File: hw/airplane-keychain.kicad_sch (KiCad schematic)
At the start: 19 parts, among them J1 CONN_01X03_MALE, SW1 SW_PUSH, SW2 SPST, U1 ATtiny85-20P

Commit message: Initial update for ISGC model
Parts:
- added R7, R8, R9: 100, Resistor_THT:R_Axial_DIN0309_L9.0mm_D3.2mm_P12.70mm_Horizontal, symbol airplane-keychain-rescue:R
- BT1, BT2: footprint Battery_Holders:Keystone_1058_1x2032-CoinCell -> Battery:BatteryHolder_Keystone_1058_1x2032
- D1: footprint LEDs:LED_D5.0mm -> LED_THT:LED_D3.0mm
- D2, D5, D6: footprint LEDs:LED_1206 -> LED_THT:LED_D3.0mm
- D3, D4: footprint LEDs:LED_D3.0mm_Horizontal_O1.27mm_Z2.0mm -> LED_THT:LED_D3.0mm
- D7: footprint LEDs:LED_D5.0mm_Horizontal_O1.27mm_Z3.0mm -> LED_THT:LED_D3.0mm
- J1: footprint Pin_Headers:Pin_Header_Straight_1x03_Pitch2.54mm -> Connector_PinHeader_2.54mm:PinHeader_1x03_P2.54mm_Horizontal
- R1, R2, R3, R4, R5, R6: footprint Resistors_THT:R_Axial_DIN0309_L9.0mm_D3.2mm_P12.70mm_Horizontal -> Resistor_THT:R_Axial_DIN0309_L9.0mm_D3.2mm_P12.70mm_Horizontal
- SW1: footprint Buttons_Switches_THT:SW_PUSH_6mm -> Button_Switch_THT:SW_PUSH_6mm
- SW2: footprint Buttons_Switches_THT:SW_Micro_SPST -> Button_Switch_THT:SW_DIP_SPSTx01_Slide_9.78x4.72mm_W7.62mm_P2.54mm
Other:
- title: Airplane Keychain -> ISGC Keychain
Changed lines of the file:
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@@
   (paper "A4")
   (title_block
-    (title "Airplane Keychain")
-    (date "2023-04-15")
-    (rev "B")
+    (title "ISGC Keychain")
+    (date "2023-12-07")
+    (rev "C")
     (company "Make to Innovate")
     (comment 1 "Matthew E. Nelson")
-    (comment 2 "High Wing PCB design")
+    (comment 2 "ISGC Badge")
   )
   (junction (at 40.64 80.01) (diameter 0) (color 0 0 0 0)
@@
       (effects (font (size 1.27 1.27)))
     )
-    (property "Footprint" "LEDs:LED_D5.0mm" (at 55.88 50.8 0)
+    (property "Footprint" "LED_THT:LED_D3.0mm" (at 55.88 50.8 0)
       (effects (font (size 1.27 1.27)) hide)
     )
@@
       (effects (font (size 1.27 1.27)))
     )
-    (property "Footprint" "LEDs:LED_1206" (at 55.88 59.69 0)
+    (property "Footprint" "LED_THT:LED_D3.0mm" (at 55.88 59.69 0)
       (effects (font (size 1.27 1.27)) hide)
     )
@@
       (effects (font (size 1.27 1.27)))
     )
-    (property "Footprint" "LEDs:LED_D3.0mm_Horizontal_O1.27mm_Z2.0mm" (at 55.88 71.12 0)
+    (property "Footprint" "LED_THT:LED_D3.0mm" (at 55.88 71.12 0)
       (effects (font (size 1.27 1.27)) hide)
     )
@@
       (effects (font (size 1.27 1.27)))
     )
-    (property "Footprint" "LEDs:LED_D3.0mm_Horizontal_O1.27mm_Z2.0mm" (at 55.88 80.01 0)
+    (property "Footprint" "LED_THT:LED_D3.0mm" (at 55.88 80.01 0)
       (effects (font (size 1.27 1.27)) hide)
     )
@@
       (effects (font (size 1.27 1.27)))
     )
-    (property "Footprint" "LEDs:LED_1206" (at 55.88 93.98 0)
+    (property "Footprint" "LED_THT:LED_D3.0mm" (at 55.88 93.98 0)
       (effects (font (size 1.27 1.27)) hide)
     )
@@
       (effects (font (size 1.27 1.27)))
     )
-    (property "Footprint" "LEDs:LED_1206" (at 55.88 102.87 0)
+    (property "Footprint" "LED_THT:LED_D3.0mm" (at 55.88 102.87 0)
       (effects (font (size 1.27 1.27)) hide)
     )
@@
       (effects (font (size 1.27 1.27)))
     )
-    (property "Footprint" "LEDs:LED_D5.0mm_Horizontal_O1.27mm_Z3.0mm" (at 55.88 116.84 0)
+    (property "Footprint" "LED_THT:LED_D3.0mm" (at 55.88 116.84 0)
       (effects (font (size 1.27 1.27)) hide)
     )
@@
       (effects (font (size 1.27 1.27)))
     )
-    (property "Footprint" "Buttons_Switches_THT:SW_PUSH_6mm" (at 106.68 116.84 0)
+    (property "Footprint" "Button_Switch_THT:SW_PUSH_6mm" (at 106.68 116.84 0)
       (effects (font (size 1.27 1.27)) hide)
     )
@@
       (effects (font (size 1.27 1.27)))
     )
-    (property "Footprint" "Buttons_Switches_THT:SW_Micro_SPST" (at 220.98 87.63 0)
+    (property "Footprint" "Button_Switch_THT:SW_DIP_SPSTx01_Slide_9.78x4.72mm_W7.62mm_P2.54mm" (at 220.98 87.63 0)
       (effects (font (size 1.27 1.27)) hide)
     )
@@
       (effects (font (size 1.27 1.27)))
     )
-    (property "Footprint" "Resistors_THT:R_Axial_DIN0309_L9.0mm_D3.2mm_P12.70mm_Horizontal" (at 74.93 49.022 90)
+    (property "Footprint" "Resistor_THT:R_Axial_DIN0309_L9.0mm_D3.2mm_P12.70mm_Horizontal" (at 74.93 49.022 90)
       (effects (font (size 1.27 1.27)) hide)
     )
@@
       (effects (font (size 1.27 1.27)))
     )
-    (property "Footprint" "Resistors_THT:R_Axial_DIN0309_L9.0mm_D3.2mm_P12.70mm_Horizontal" (at 74.93 57.912 90)
+    (property "Footprint" "Resistor_THT:R_Axial_DIN0309_L9.0mm_D3.2mm_P12.70mm_Horizontal" (at 74.93 57.912 90)
       (effects (font (size 1.27 1.27)) hide)
     )
@@
       (effects (font (size 1.27 1.27)))
     )
-    (property "Footprint" "Resistors_THT:R_Axial_DIN0309_L9.0mm_D3.2mm_P12.70mm_Horizontal" (at 74.93 69.342 90)
+    (property "Footprint" "Resistor_THT:R_Axial_DIN0309_L9.0mm_D3.2mm_P12.70mm_Horizontal" (at 74.93 69.342 90)
       (effects (font (size 1.27 1.27)) hide)
     )
@@
       (effects (font (size 1.27 1.27)))
     )
-    (property "Footprint" "Resistors_THT:R_Axial_DIN0309_L9.0mm_D3.2mm_P12.70mm_Horizontal" (at 74.93 78.232 90)
+    (property "Footprint" "Resistor_THT:R_Axial_DIN0309_L9.0mm_D3.2mm_P12.70mm_Horizontal" (at 74.93 78.232 90)
       (effects (font (size 1.27 1.27)) hide)
     )
@@
       (effects (font (size 1.27 1.27)))
     )
-    (property "Footprint" "Resistors_THT:R_Axial_DIN0309_L9.0mm_D3.2mm_P12.70mm_Horizontal" (at 74.93 115.062 90)
+    (property "Footprint" "Resistor_THT:R_Axial_DIN0309_L9.0mm_D3.2mm_P12.70mm_Horizontal" (at 74.93 115.062 90)
       (effects (font (size 1.27 1.27)) hide)
     )
@@
       (effects (font (size 1.27 1.27)) (justify left))
     )
-    (property "Footprint" "Battery_Holders:Keystone_1058_1x2032-CoinCell" (at 234.95 117.856 90)
+    (property "Footprint" "Battery:BatteryHolder_Keystone_1058_1x2032" (at 234.95 117.856 90)
       (effects (font (size 1.27 1.27)) hide)
     )
@@
       (effects (font (size 1.27 1.27)) (justify left))
     )
-    (property "Footprint" "Battery_Holders:Keystone_1058_1x2032-CoinCell" (at 220.98 117.856 90)
+    (property "Footprint" "Battery:BatteryHolder_Keystone_1058_1x2032" (at 220.98 117.856 90)
       (effects (font (size 1.27 1.27)) hide)
     )
@@
       (effects (font (size 1.27 1.27)))
     )
-    (property "Footprint" "Pin_Headers:Pin_Header_Straight_1x03_Pitch2.54mm" (at 48.26 26.67 0)
+    (property "Footprint" "Connector_PinHeader_2.54mm:PinHeader_1x03_P2.54mm_Horizontal" (at 48.26 26.67 0)
       (effects (font (size 1.27 1.27)) hide)
     )
@@
       (effects (font (size 1.27 1.27)))
     )
-    (property "Footprint" "Resistors_THT:R_Axial_DIN0309_L9.0mm_D3.2mm_P12.70mm_Horizontal" (at 161.29 99.822 90)
+    (property "Footprint" "Resistor_THT:R_Axial_DIN0309_L9.0mm_D3.2mm_P12.70mm_Horizontal" (at 161.29 99.822 90)
       (effects (font (size 1.27 1.27)) hide)
     )
@@
         (path "/6cfc2c66-5048-4a9e-b97d-b82fde315677"
           (reference "R6") (unit 1)
+        )
+      )
+    )
+  )
+  (symbol (lib_id "airplane-keychain-rescue:R") (at 73.66 105.41 270) (unit 1)
+    (in_bom yes) (on_board yes) (dnp no)
+    (property "Reference" "R8" (at 73.66 107.442 90)
+      (effects (font (size 1.27 1.27)))
+    )
+    (property "Value" "100" (at 73.66 105.41 90)
+      (effects (font (size 1.27 1.27)))
+    )
+    (property "Footprint" "Resistor_THT:R_Axial_DIN0309_L9.0mm_D3.2mm_P12.70mm_Horizontal" (at 73.66 103.632 90)
+      (effects (font (size 1.27 1.27)) hide)
+    )
+    (property "Datasheet" "" (at 73.66 105.41 0)
+      (effects (font (size 1.27 1.27)) hide)
+    )
+    (pin "1")
+    (pin "2")
+    (instances
+      (project "airplane-keychain"
+        (path "/6cfc2c66-5048-4a9e-b97d-b82fde315677"
+          (reference "R8") (unit 1)
+        )
+      )
+    )
+  )
+  (symbol (lib_id "airplane-keychain-rescue:R") (at 74.93 123.19 270) (unit 1)
+    (in_bom yes) (on_board yes) (dnp no)
+    (property "Reference" "R9" (at 74.93 125.222 90)
+      (effects (font (size 1.27 1.27)))
+    )
+    (property "Value" "100" (at 74.93 123.19 90)
+      (effects (font (size 1.27 1.27)))
+    )
+    (property "Footprint" "Resistor_THT:R_Axial_DIN0309_L9.0mm_D3.2mm_P12.70mm_Horizontal" (at 74.93 121.412 90)
+      (effects (font (size 1.27 1.27)) hide)
+    )
+    (property "Datasheet" "" (at 74.93 123.19 0)
+      (effects (font (size 1.27 1.27)) hide)
+    )
+    (pin "1")
+    (pin "2")
+    (instances
+      (project "airplane-keychain"
+        (path "/6cfc2c66-5048-4a9e-b97d-b82fde315677"
+          (reference "R9") (unit 1)
         )
       )
@@
         )
       )
+    )
+  )
+  (symbol (lib_id "airplane-keychain-rescue:R") (at 72.39 91.44 270) (unit 1)
+    (in_bom yes) (on_board yes) (dnp no)
+    (property "Reference" "R7" (at 72.39 93.472 90)
+      (effects (font (size 1.27 1.27)))
+    )
+    (property "Value" "100" (at 72.39 91.44 90)
+      (effects (font (size 1.27 1.27)))
+    )
+    (property "Footprint" "Resistor_THT:R_Axial_DIN0309_L9.0mm_D3.2mm_P12.70mm_Horizontal" (at 72.39 89.662 90)
+      (effects (font (size 1.27 1.27)) hide)
+    )
+    (property "Datasheet" "" (at 72.39 91.44 0)
+      (effects (font (size 1.27 1.27)) hide)
+    )
+    (pin "1")
+    (pin "2")
+    (instances
+      (project "airplane-keychain"
+        (path "/6cfc2c66-5048-4a9e-b97d-b82fde315677"
+          (reference "R7") (unit 1)
+        )
+      )

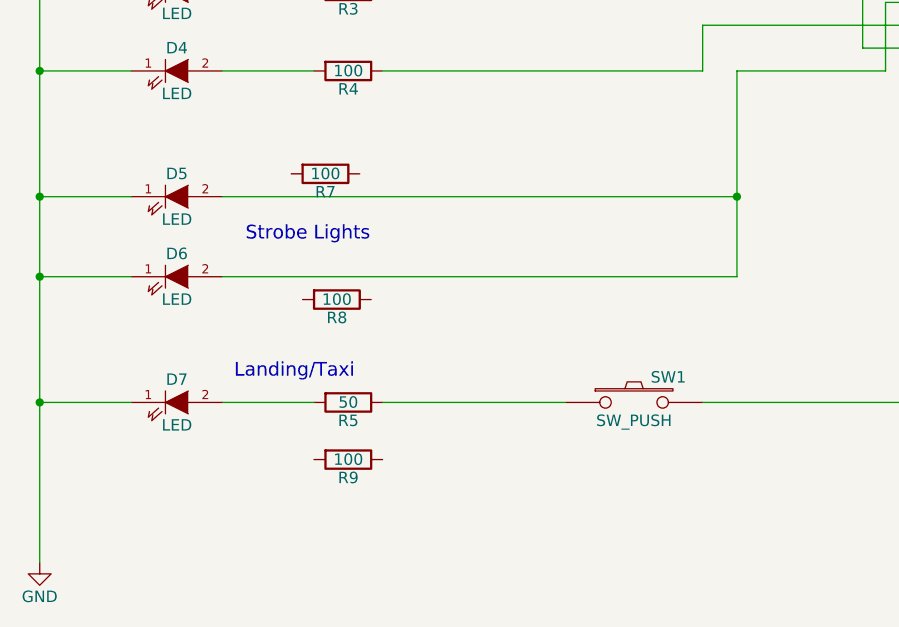
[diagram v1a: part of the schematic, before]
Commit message: Updates to logo
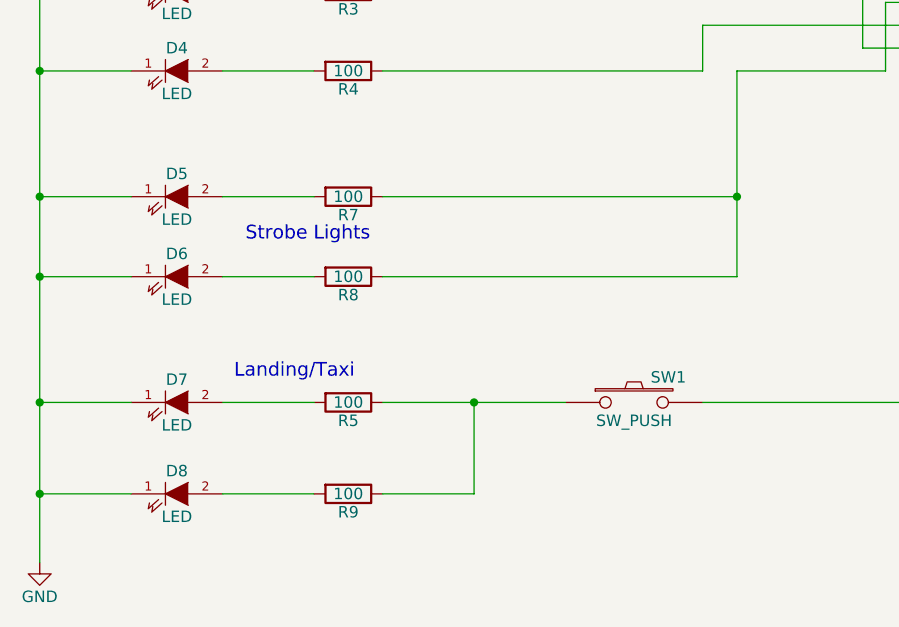
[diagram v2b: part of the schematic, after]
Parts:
- added D8: LED, LED_THT:LED_D3.0mm, symbol airplane-keychain-rescue:LED-RESCUE-airplane-keychain
- R5: value 50 -> 100
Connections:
- net GND: now also D8.1 (K)
- net at R5.1, SW1.1: now also R9.1
- net at R8.1: now also R7.1, U1.3 (XTAL2/PB4)
- net at R8.2: now also D6.2 (A)
- net at R9.2: now also D8.2 (A)
- net at R7.2: now also D5.2 (A)
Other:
- moved on the sheet: R7, R8, R9

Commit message: Update for ISGC
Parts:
- removed J1: CONN_01X03_MALE, Connector_PinHeader_2.54mm:PinHeader_1x03_P2.54mm_Horizontal, symbol airplane-keychain-rescue:CONN_01X03_MALE
- added H1: MountingHole, MountingHole:MountingHole_4.3mm_M4, symbol Mechanical:MountingHole
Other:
- note removed: "Optional Tail Header"
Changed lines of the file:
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@@
   (junction (at 40.64 80.01) (diameter 0) (color 0 0 0 0)
   )
-  (junction (at 63.5 50.8) (diameter 0) (color 0 0 0 0)
-  )
   (junction (at 40.64 59.69) (diameter 0) (color 0 0 0 0)
   )
@@
   (junction (at 40.64 71.12) (diameter 0) (color 0 0 0 0)
   )
-  (junction (at 40.64 50.8) (diameter 0) (color 0 0 0 0)
-  )
   (junction (at 118.11 93.98) (diameter 0) (color 0 0 0 0)
   )
@@
   (junction (at 40.64 93.98) (diameter 0) (color 0 0 0 0)
   )
-  (junction (at 68.58 59.69) (diameter 0) (color 0 0 0 0)
-  )
   (junction (at 220.98 107.95) (diameter 0) (color 0 0 0 0)
   )
@@
     (stroke (width 0) (type default))
   )
-  (wire (pts (xy 60.96 50.8) (xy 63.5 50.8))
+  (wire (pts (xy 60.96 50.8) (xy 71.12 50.8))
     (stroke (width 0) (type default))
   )
@@
     (stroke (width 0) (type default))
   )
-  (wire (pts (xy 55.88 31.75) (xy 58.42 31.75))
-    (stroke (width 0) (type default))
-  )
   (wire (pts (xy 118.11 93.98) (xy 118.11 102.87))
     (stroke (width 0) (type default))
@@
     (stroke (width 0) (type default))
   )
-  (wire (pts (xy 55.88 36.83) (xy 63.5 36.83))
-    (stroke (width 0) (type default))
-  )
   (wire (pts (xy 132.08 77.47) (xy 132.08 71.12))
     (stroke (width 0) (type default))
@@
     (stroke (width 0) (type default))
   )
-  (wire (pts (xy 63.5 36.83) (xy 63.5 50.8))
-    (stroke (width 0) (type default))
-  )
   (wire (pts (xy 207.01 90.17) (xy 207.01 101.6))
     (stroke (width 0) (type default))
@@
     (stroke (width 0) (type default))
   )
-  (wire (pts (xy 58.42 31.75) (xy 58.42 34.29))
-    (stroke (width 0) (type default))
-  )
   (wire (pts (xy 146.05 77.47) (xy 132.08 77.47))
     (stroke (width 0) (type default))
@@
     (stroke (width 0) (type default))
   )
-  (wire (pts (xy 60.96 59.69) (xy 68.58 59.69))
+  (wire (pts (xy 60.96 59.69) (xy 71.12 59.69))
     (stroke (width 0) (type default))
   )
@@
     (stroke (width 0) (type default))
   )
-  (wire (pts (xy 55.88 26.67) (xy 68.58 26.67))
-    (stroke (width 0) (type default))
-  )
-  (wire (pts (xy 40.64 34.29) (xy 40.64 50.8))
-    (stroke (width 0) (type default))
-  )
   (wire (pts (xy 78.74 71.12) (xy 132.08 71.12))
     (stroke (width 0) (type default))
   )
-  (wire (pts (xy 68.58 26.67) (xy 68.58 59.69))
-    (stroke (width 0) (type default))
-  )
   (wire (pts (xy 161.29 54.61) (xy 161.29 59.69))
     (stroke (width 0) (type default))
@@
     (stroke (width 0) (type default))
   )
-  (wire (pts (xy 68.58 59.69) (xy 71.12 59.69))
-    (stroke (width 0) (type default))
-  )
   (wire (pts (xy 165.1 101.6) (xy 207.01 101.6))
     (stroke (width 0) (type default))
@@
     (stroke (width 0) (type default))
   )
-  (wire (pts (xy 63.5 50.8) (xy 71.12 50.8))
-    (stroke (width 0) (type default))
-  )
   (wire (pts (xy 207.01 69.85) (xy 220.98 69.85))
     (stroke (width 0) (type default))
@@
   )
   (wire (pts (xy 60.96 116.84) (xy 71.12 116.84))
-    (stroke (width 0) (type default))
-  )
-  (wire (pts (xy 58.42 34.29) (xy 40.64 34.29))
     (stroke (width 0) (type default))
   )
@@
     (effects (font (size 1.524 1.524)) (justify left bottom))
   )
-  (text "Optional Tail Header" (at 57.15 24.13 0)
-    (effects (font (size 1.524 1.524)) (justify left bottom))
-  )
   (text "Beacon" (at 60.96 48.26 0)
     (effects (font (size 1.524 1.524)) (justify left bottom))
@@
     )
   )
-  (symbol (lib_id "airplane-keychain-rescue:CONN_01X03_MALE") (at 48.26 31.75 0) (unit 1)
-    (in_bom yes) (on_board yes) (dnp no)
-    (property "Reference" "J1" (at 48.26 24.765 0)
-      (effects (font (size 1.27 1.27)))
-    )
-    (property "Value" "CONN_01X03_MALE" (at 48.895 38.735 0)
-      (effects (font (size 1.27 1.27)))
-    )
-    (property "Footprint" "Connector_PinHeader_2.54mm:PinHeader_1x03_P2.54mm_Horizontal" (at 48.26 26.67 0)
-      (effects (font (size 1.27 1.27)) hide)
-    )
-    (property "Datasheet" "" (at 48.26 26.67 0)
-      (effects (font (size 1.27 1.27)) hide)
-    )
-    (pin "1")
-    (pin "2")
-    (pin "3")
-    (instances
-      (project "airplane-keychain"
-        (path "/6cfc2c66-5048-4a9e-b97d-b82fde315677"
-          (reference "J1") (unit 1)
-        )
-      )
-    )
-  )
   (symbol (lib_id "airplane-keychain-rescue:R") (at 161.29 101.6 270) (unit 1)
     (in_bom yes) (on_board yes) (dnp no)
@@
         )
       )
+    )
+  )
+  (symbol (lib_id "Mechanical:MountingHole") (at 40.64 157.48 0) (unit 1)
+    (in_bom yes) (on_board yes) (dnp no) (fields_autoplaced)
+    (property "Reference" "H1" (at 43.18 156.21 0)
+      (effects (font (size 1.27 1.27)) (justify left))
+    )
+    (property "Value" "MountingHole" (at 43.18 158.75 0)
+      (effects (font (size 1.27 1.27)) (justify left))
+    )
+    (property "Footprint" "MountingHole:MountingHole_4.3mm_M4" (at 40.64 157.48 0)
+      (effects (font (size 1.27 1.27)) hide)
+    )
+    (property "Datasheet" "~" (at 40.64 157.48 0)
+      (effects (font (size 1.27 1.27)) hide)
+    )
+    (instances
+      (project "airplane-keychain"
+        (path "/6cfc2c66-5048-4a9e-b97d-b82fde315677"
+          (reference "H1") (unit 1)
+        )
+      )

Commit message: Updates
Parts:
- added D9: LED, LED_THT:LED_D3.0mm, symbol airplane-keychain-rescue:LED-RESCUE-airplane-keychain
- added R10: 100, Resistor_THT:R_Axial_DIN0309_L9.0mm_D3.2mm_P12.70mm_Horizontal, symbol airplane-keychain-rescue:R
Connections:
- net GND: now also D9.1 (K)
- net at R5.1, R9.1, SW1.1: now also R10.1
- new net: D9.2 (A), R10.2
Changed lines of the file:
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@@
   (junction (at 40.64 59.69) (diameter 0) (color 0 0 0 0)
   )
+  (junction (at 40.64 133.35) (diameter 0) (color 0 0 0 0)
+  )
   (junction (at 40.64 102.87) (diameter 0) (color 0 0 0 0)
   )
   (junction (at 40.64 71.12) (diameter 0) (color 0 0 0 0)
   )
+  (junction (at 88.9 127) (diameter 0) (color 0 0 0 0)
+  )
   (junction (at 118.11 93.98) (diameter 0) (color 0 0 0 0)
   )
@@
     (stroke (width 0) (type default))
   )
+  (wire (pts (xy 88.9 133.35) (xy 88.9 127))
+    (stroke (width 0) (type default))
+  )
   (wire (pts (xy 146.05 69.85) (xy 139.7 69.85))
     (stroke (width 0) (type default))
@@
     (stroke (width 0) (type default))
   )
-  (wire (pts (xy 40.64 127) (xy 40.64 134.62))
+  (wire (pts (xy 40.64 127) (xy 40.64 133.35))
     (stroke (width 0) (type default))
   )
@@
     (stroke (width 0) (type default))
   )
+  (wire (pts (xy 50.8 133.35) (xy 40.64 133.35))
+    (stroke (width 0) (type default))
+  )
   (wire (pts (xy 220.98 69.85) (xy 220.98 74.93))
     (stroke (width 0) (type default))
@@
     (stroke (width 0) (type default))
   )
+  (wire (pts (xy 60.96 133.35) (xy 71.12 133.35))
+    (stroke (width 0) (type default))
+  )
+  (wire (pts (xy 78.74 133.35) (xy 88.9 133.35))
+    (stroke (width 0) (type default))
+  )
   (wire (pts (xy 207.01 69.85) (xy 220.98 69.85))
     (stroke (width 0) (type default))
@@
   )
   (wire (pts (xy 118.11 80.01) (xy 118.11 93.98))
+    (stroke (width 0) (type default))
+  )
+  (wire (pts (xy 40.64 133.35) (xy 40.64 134.62))
     (stroke (width 0) (type default))
   )
@@
         (path "/6cfc2c66-5048-4a9e-b97d-b82fde315677"
           (reference "R8") (unit 1)
+        )
+      )
+    )
+  )
+  (symbol (lib_id "airplane-keychain-rescue:LED-RESCUE-airplane-keychain") (at 55.88 133.35 0) (unit 1)
+    (in_bom yes) (on_board yes) (dnp no)
+    (property "Reference" "D9" (at 55.88 130.81 0)
+      (effects (font (size 1.27 1.27)))
+    )
+    (property "Value" "LED" (at 55.88 135.89 0)
+      (effects (font (size 1.27 1.27)))
+    )
+    (property "Footprint" "LED_THT:LED_D3.0mm" (at 55.88 133.35 0)
+      (effects (font (size 1.27 1.27)) hide)
+    )
+    (property "Datasheet" "" (at 55.88 133.35 0)
+      (effects (font (size 1.27 1.27)))
+    )
+    (pin "1")
+    (pin "2")
+    (instances
+      (project "airplane-keychain"
+        (path "/6cfc2c66-5048-4a9e-b97d-b82fde315677"
+          (reference "D9") (unit 1)
         )
       )
@@
         )
       )
+    )
+  )
+  (symbol (lib_id "airplane-keychain-rescue:R") (at 74.93 133.35 270) (unit 1)
+    (in_bom yes) (on_board yes) (dnp no)
+    (property "Reference" "R10" (at 74.93 135.382 90)
+      (effects (font (size 1.27 1.27)))
+    )
+    (property "Value" "100" (at 74.93 133.35 90)
+      (effects (font (size 1.27 1.27)))
+    )
+    (property "Footprint" "Resistor_THT:R_Axial_DIN0309_L9.0mm_D3.2mm_P12.70mm_Horizontal" (at 74.93 131.572 90)
+      (effects (font (size 1.27 1.27)) hide)
+    )
+    (property "Datasheet" "" (at 74.93 133.35 0)
+      (effects (font (size 1.27 1.27)) hide)
+    )
+    (pin "1")
+    (pin "2")
+    (instances
+      (project "airplane-keychain"
+        (path "/6cfc2c66-5048-4a9e-b97d-b82fde315677"
+          (reference "R10") (unit 1)
+        )
+      )

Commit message: Minor edits to page details
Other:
- note added: "Blinky Stars"
- note added: "Fading Star"
- note added: "Fading Stars"
- note added: "Push Button Stars"
- note removed: "Beacon"
- note removed: "Landing/Taxi"
- note removed: "Strobe Lights"
- note removed: "Tail"
